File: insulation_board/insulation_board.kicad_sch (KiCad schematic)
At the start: 26 parts, among them IC1 LTV-846S, J1 Conn_01x06, J2 110990030, J3 Conn_02x03_Odd_Even, J4 110990030, Q1 BSS84DW-7-F, Q2 BSS84DW-7-F

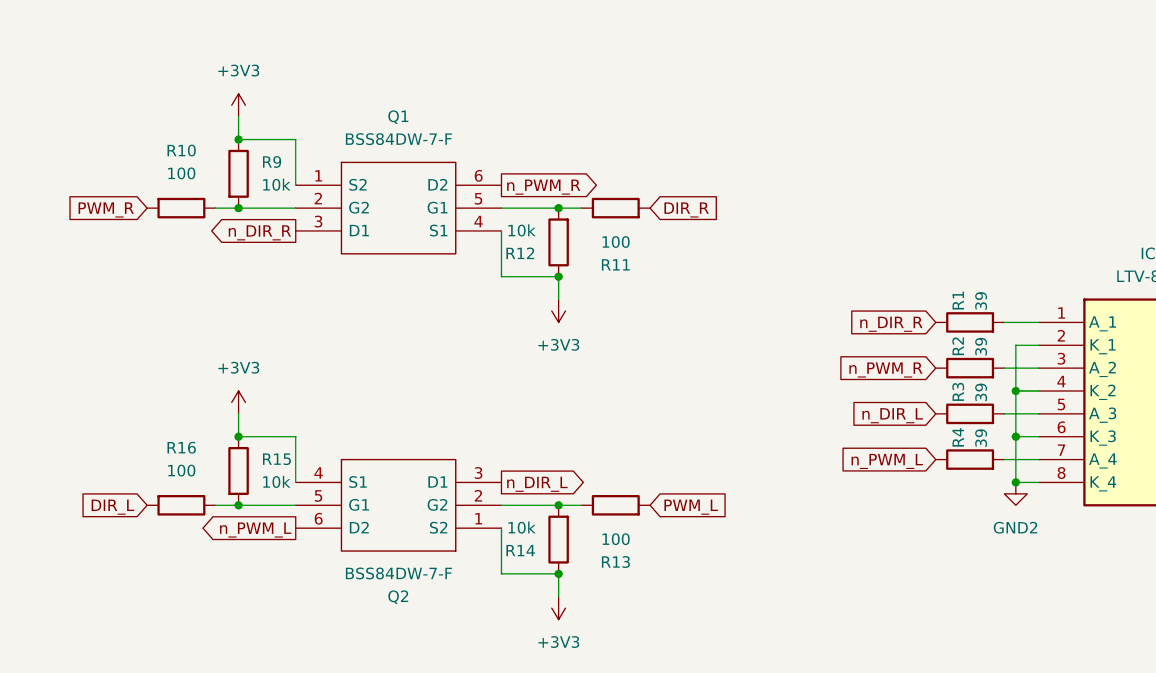
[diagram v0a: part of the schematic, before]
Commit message: 非常停止スイッチを追加
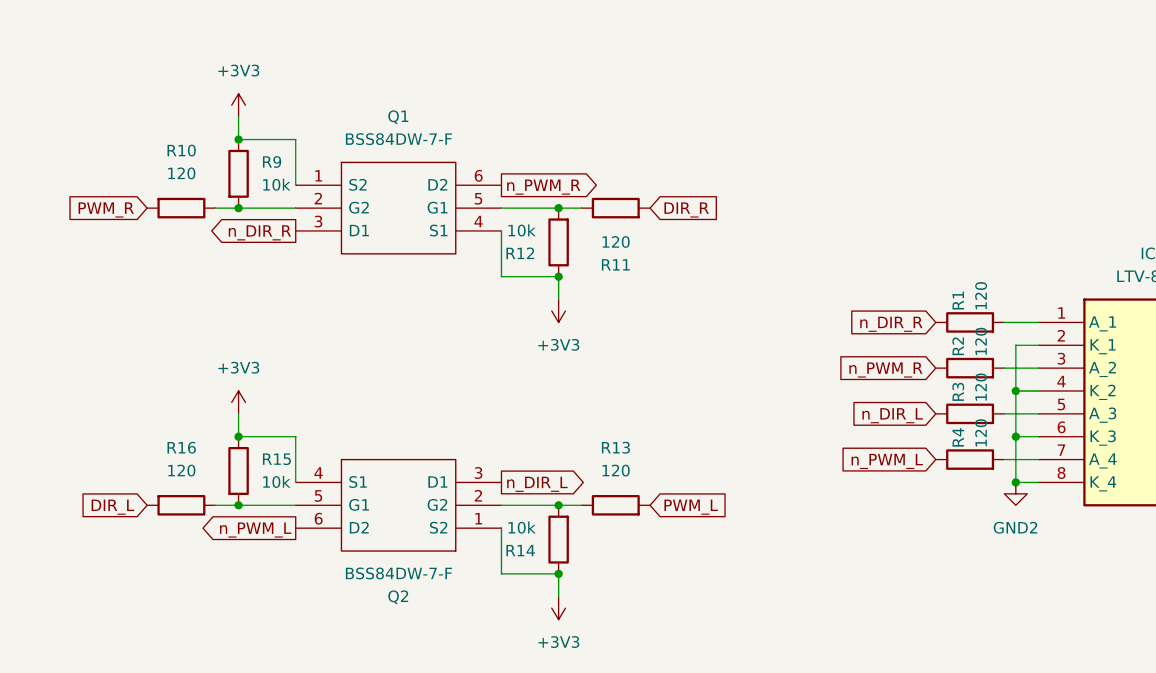
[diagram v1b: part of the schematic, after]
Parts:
- R1, R2, R3, R4: value 39 -> 120
- R10, R11, R13, R16: value 100 -> 120
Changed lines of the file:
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@@
 			)
 		)
-		(property "Value" "39"
+		(property "Value" "120"
 			(at 157.48 133.35 0)
 			(effects
@@
 			)
 		)
-		(property "Value" "39"
+		(property "Value" "120"
 			(at 157.48 143.51 0)
 			(effects
@@
 			)
 		)
-		(property "Value" "100"
+		(property "Value" "120"
 			(at 116.84 120.65 90)
 			(effects
@@
 			)
 		)
-		(property "Value" "39"
+		(property "Value" "120"
 			(at 157.48 128.27 0)
 			(effects
@@
 			)
 		)
-		(property "Value" "100"
+		(property "Value" "120"
 			(at 68.58 113.03 90)
 			(effects
@@
 			)
 		)
-		(property "Value" "100"
+		(property "Value" "120"
 			(at 68.58 146.05 90)
 			(effects
@@
 			)
 		)
-		(property "Value" "39"
+		(property "Value" "120"
 			(at 157.48 138.43 0)
 			(effects
@@
 		(fields_autoplaced yes)
 		(property "Reference" "R13"
-			(at 116.84 156.21 90)
+			(at 116.84 143.51 90)
 			(effects
 				(font
@@
 			)
 		)
-		(property "Value" "100"
-			(at 116.84 153.67 90)
+		(property "Value" "120"
+			(at 116.84 146.05 90)
 			(effects
 				(font
